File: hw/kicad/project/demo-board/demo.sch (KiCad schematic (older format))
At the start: 2 parts

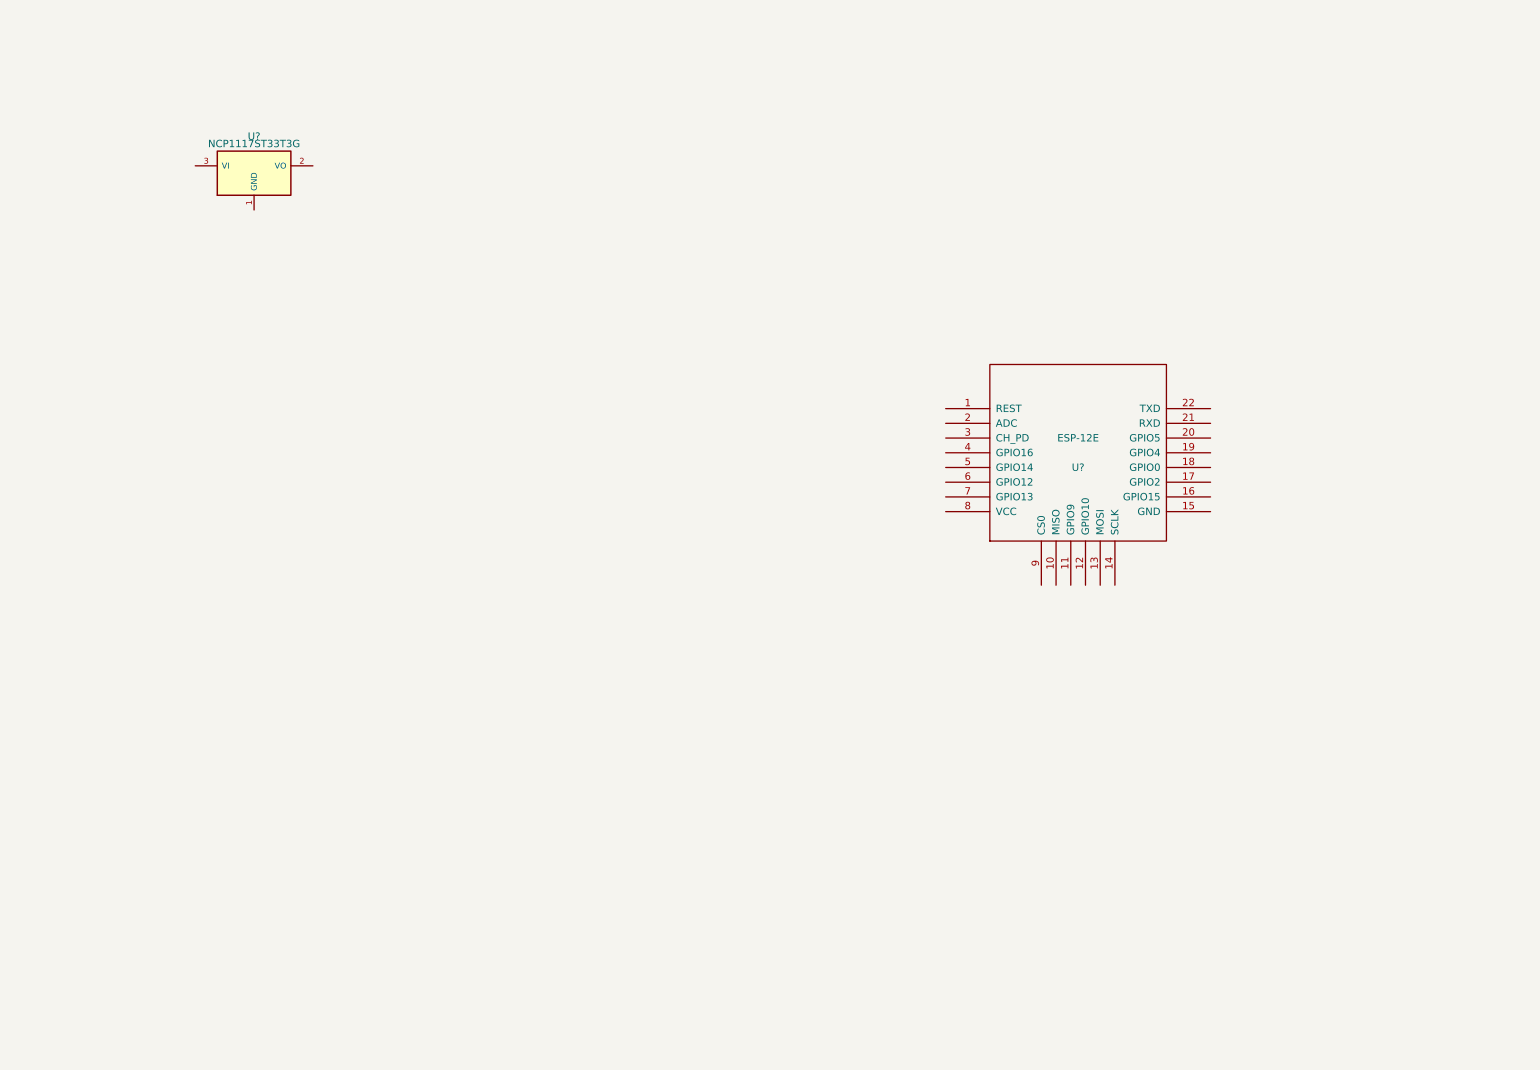
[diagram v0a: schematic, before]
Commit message: Demo schema for ESP connections
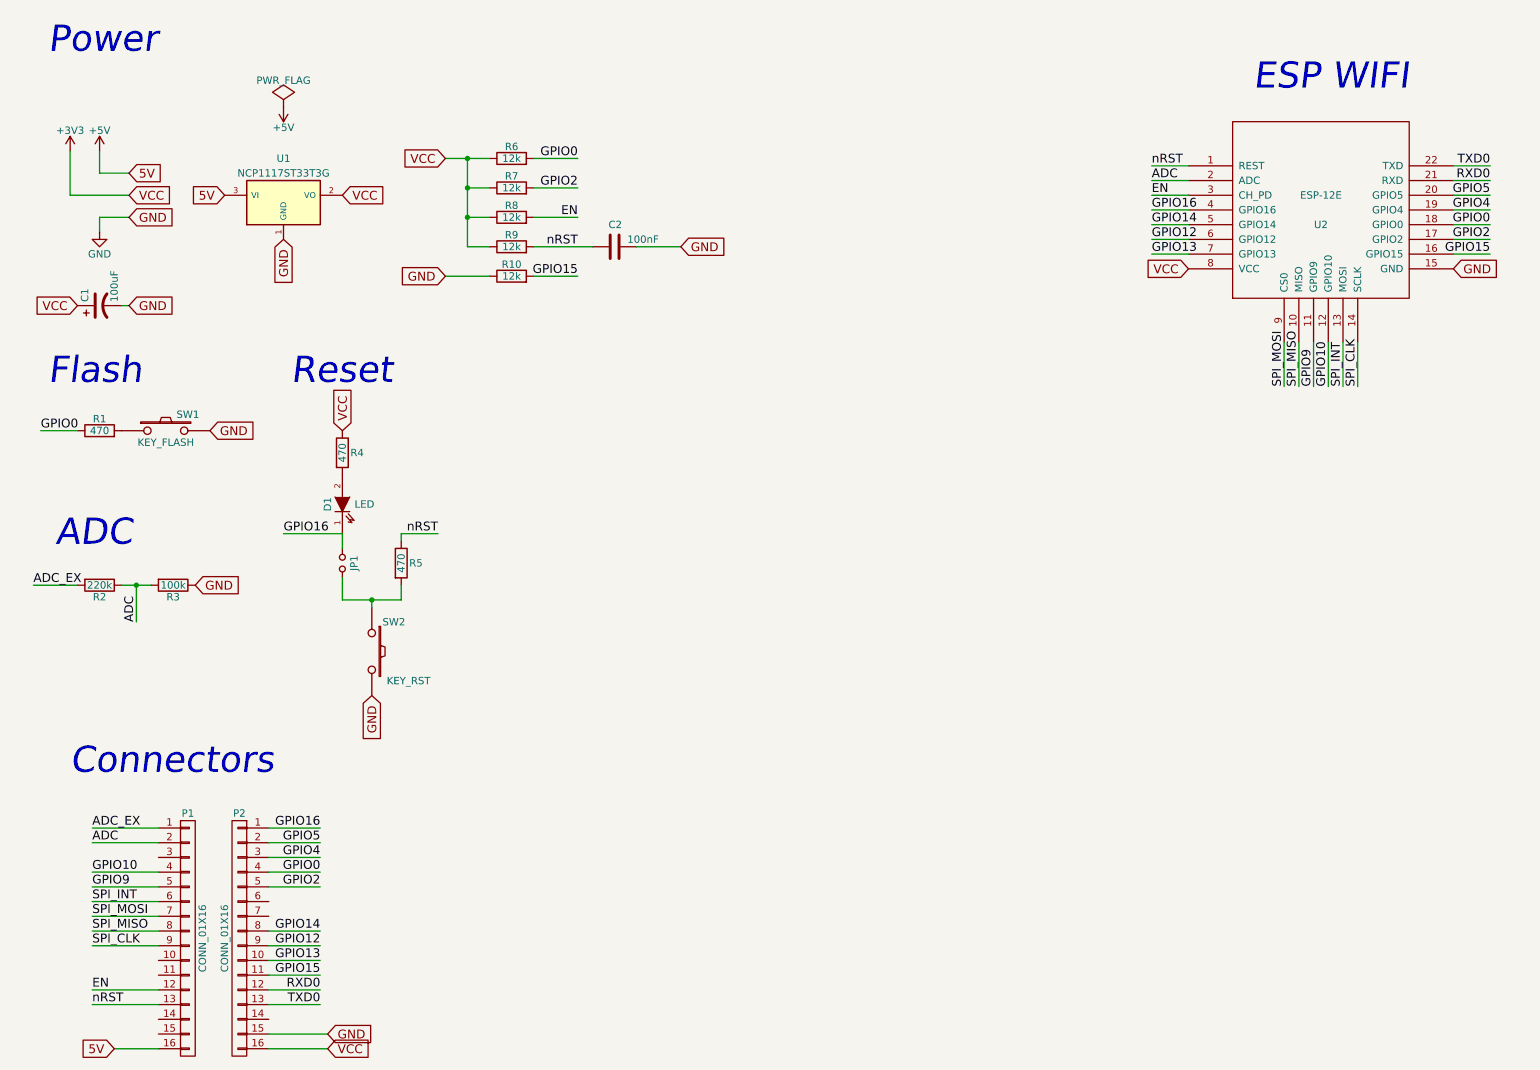
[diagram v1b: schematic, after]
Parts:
- added C1: 100uF, symbol CP1
- added C2: 100nF, symbol C
- added D1: LED, symbol LED
- added JP1: Jumper_NO_Small, symbol Jumper_NO_Small
- added P1, P2: CONN_01X16, symbol CONN_01X16
- added R1, R4, R5: 470, symbol R
- added R10, R6, R7, R8, R9: 12k, symbol R
- added R2: 220k, symbol R
- added R3: 100k, symbol R
- added SW1: KEY_FLASH, symbol SW_PUSH
- added SW2: KEY_RST, symbol SW_PUSH
- gave numbers to parts that had none: 2
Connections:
- net nRST: now reaches U2.1 (REST)
- net nRST: now also C2.1, P1.13 (P13), R5.1, R9.2
- net SPI_MISO: now reaches U2.10 (MISO)
- net SPI_MISO: now also P1.8 (P8)
- net GPIO9: now reaches U2.11 (GPIO9)
- net GPIO9: now also P1.5 (P5)
- net GPIO10: now reaches U2.12 (GPIO10)
- net GPIO10: now also P1.4 (P4)
- net SPI_INT: now reaches U2.13 (MOSI)
- net SPI_INT: now also P1.6 (P6)
- net SPI_CLK: now reaches U2.14 (SCLK)
- net SPI_CLK: now also P1.9 (P9)
- net GND: now reaches U2.15 (GND)
- net GND: now also U1.1 (GND), C1.2, C2.2, P2.15 (P15), R10.1, R3.1, SW1.2, SW2.2
- net GPIO15: now reaches U2.16 (GPIO15)
- net GPIO15: now also P2.11 (P11), R10.2
- net GPIO2: now reaches U2.17 (GPIO2)
- net GPIO2: now also P2.5 (P5), R7.2
- net GPIO0: now reaches U2.18 (GPIO0)
- net GPIO0: now also P2.4 (P4), R1.1, R6.2
- net GPIO4: now reaches U2.19 (GPIO4)
- net GPIO4: now also P2.3 (P3)
- net ADC: now reaches U2.2 (ADC)
- net ADC: now also P1.2 (P2), R2.1, R3.2
- net GPIO5: now reaches U2.20 (GPIO5)
- net GPIO5: now also P2.2 (P2)
- net RXD0: now reaches U2.21 (RXD)
- net RXD0: now also P2.12 (P12)
- net TXD0: now reaches U2.22 (TXD)
- net TXD0: now also P2.13 (P13)
- net EN: now reaches U2.3 (CH_PD)
- net EN: now also P1.12 (P12), R8.2
- net GPIO16: now reaches U2.4 (GPIO16)
- net GPIO16: now also D1.1 (K), JP1.1, P2.1 (P1)
- net GPIO14: now reaches U2.5 (GPIO14)
- net GPIO14: now also P2.8 (P8)
- net GPIO12: now reaches U2.6 (GPIO12)
- net GPIO12: now also P2.9 (P9)
- net GPIO13: now reaches U2.7 (GPIO13)
- net GPIO13: now also P2.10 (P10)
- net +3V3: now reaches U2.8 (VCC)
- net +3V3: now also U1.2 (VO), C1.1, P2.16 (P16), R4.1, R6.1, R7.1, R8.1, R9.1
- net SPI_MOSI: now reaches U2.9 (CS0)
- net SPI_MOSI: now also P1.7 (P7)
- net +5V: now reaches U1.3 (VI)
- net +5V: now also P1.16 (P16)
- new net: R1.2, SW1.1
- new net: D1.2 (A), R4.2
- new net: JP1.2, R5.2, SW2.1
- new net ADC_EX: P1.1 (P1), R2.2
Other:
- note added: "ADC\n"
- note added: "Connectors"
- note added: "ESP WIFI"
- note added: "Flash"
- note added: "Power"
- note added: "Reset"
- moved on the sheet: U1, U2

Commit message: Parts associated
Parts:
- C1: footprint (none) -> Capacitors_Tantalum_SMD:TantalC_SizeB_EIA-3528_Reflow
- C2: footprint (none) -> Capacitors_SMD:C_0402
- D1: footprint (none) -> LEDs:LED-1206
- JP1: footprint (none) -> Pin_Headers:Pin_Header_Straight_1x02
- P1, P2: footprint (none) -> Pin_Headers:Pin_Header_Straight_1x16
- R1, R10, R2, R3, R4, R5, R6, R7, R8, R9: footprint (none) -> Resistors_SMD:R_1206
- SW1, SW2: footprint (none) -> Buttons_Switches_ThroughHole:SW_PUSH-12mm
- U1: footprint (none) -> TO_SOT_Packages_SMD:SOT-223
- U2: footprint (none) -> ESP8266:ESP-12E
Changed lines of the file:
@@
 F 0 "U2" H 9450 1850 50  0000 C CNN
 F 1 "ESP-12E" H 9450 2050 50  0000 C CNN
-F 2 "" H 9450 1950 50  0001 C CNN
+F 2 "ESP8266:ESP-12E" H 9450 1950 50  0001 C CNN
 F 3 "" H 9450 1950 50  0001 C CNN
 	1    9450 1950
@@
 F 0 "U1" H 2400 2200 50  0000 C CNN
 F 1 "NCP1117ST33T3G" H 2400 2100 50  0000 C CNN
-F 2 "" H 2400 1900 50  0000 C CNN
+F 2 "TO_SOT_Packages_SMD:SOT-223" H 2400 1900 50  0001 C CNN
 F 3 "" H 2400 1900 50  0000 C CNN
 	1    2400 1900
@@
 F 0 "R6" V 4030 1600 50  0000 C CNN
 F 1 "12k" V 3950 1600 50  0000 C CNN
-F 2 "" V 3880 1600 50  0000 C CNN
+F 2 "Resistors_SMD:R_1206" V 3880 1600 50  0001 C CNN
 F 3 "" H 3950 1600 50  0000 C CNN
 	1    3950 1600
@@
 F 0 "R7" V 4030 1800 50  0000 C CNN
 F 1 "12k" V 3950 1800 50  0000 C CNN
-F 2 "" V 3880 1800 50  0000 C CNN
+F 2 "Resistors_SMD:R_1206" V 3880 1800 50  0001 C CNN
 F 3 "" H 3950 1800 50  0000 C CNN
 	1    3950 1800
@@
 F 0 "R8" V 4030 2000 50  0000 C CNN
 F 1 "12k" V 3950 2000 50  0000 C CNN
-F 2 "" V 3880 2000 50  0000 C CNN
+F 2 "Resistors_SMD:R_1206" V 3880 2000 50  0001 C CNN
 F 3 "" H 3950 2000 50  0000 C CNN
 	1    3950 2000
@@
 F 0 "R9" V 4030 2200 50  0000 C CNN
 F 1 "12k" V 3950 2200 50  0000 C CNN
-F 2 "" V 3880 2200 50  0000 C CNN
+F 2 "Resistors_SMD:R_1206" V 3880 2200 50  0001 C CNN
 F 3 "" H 3950 2200 50  0000 C CNN
 	1    3950 2200
@@
 F 0 "R10" V 4030 2400 50  0000 C CNN
 F 1 "12k" V 3950 2400 50  0000 C CNN
-F 2 "" V 3880 2400 50  0000 C CNN
+F 2 "Resistors_SMD:R_1206" V 3880 2400 50  0001 C CNN
 F 3 "" H 3950 2400 50  0000 C CNN
 	1    3950 2400
@@
 F 0 "C1" H 1175 2700 50  0000 L CNN
 F 1 "100uF" H 1175 2500 50  0000 L CNN
-F 2 "" H 1150 2600 50  0000 C CNN
+F 2 "Capacitors_Tantalum_SMD:TantalC_SizeB_EIA-3528_Reflow" H 1150 2600 50  0001 C CNN
 F 3 "" H 1150 2600 50  0000 C CNN
 	1    1150 2600
@@
 F 0 "R1" V 1230 3450 50  0000 C CNN
 F 1 "470" V 1150 3450 50  0000 C CNN
-F 2 "" V 1080 3450 50  0000 C CNN
+F 2 "Resistors_SMD:R_1206" V 1080 3450 50  0001 C CNN
 F 3 "" H 1150 3450 50  0000 C CNN
 	1    1150 3450
@@
 F 0 "SW1" H 1750 3560 50  0000 C CNN
 F 1 "KEY_FLASH" H 1600 3370 50  0000 C CNN
-F 2 "" H 1600 3450 50  0000 C CNN
+F 2 "Buttons_Switches_ThroughHole:SW_PUSH-12mm" H 1600 3450 50  0001 C CNN
 F 3 "" H 1600 3450 50  0000 C CNN
 	1    1600 3450
@@
 F 0 "R4" H 2900 3600 50  0000 C CNN
 F 1 "470" V 2800 3600 50  0000 C CNN
-F 2 "" V 2730 3600 50  0000 C CNN
+F 2 "Resistors_SMD:R_1206" V 2730 3600 50  0001 C CNN
 F 3 "" H 2800 3600 50  0000 C CNN
 	1    2800 3600
@@
 F 0 "D1" H 2800 4050 50  0000 C CNN
 F 1 "LED" V 2800 3800 50  0000 C CNN
-F 2 "" H 2800 3950 50  0000 C CNN
+F 2 "LEDs:LED-1206" H 2800 3950 50  0001 C CNN
 F 3 "" H 2800 3950 50  0000 C CNN
 	1    2800 3950
@@
 F 0 "JP1" H 2800 4430 50  0000 C CNN
 F 1 "Jumper_NO_Small" H 2810 4290 50  0001 C CNN
-F 2 "" H 2800 4350 50  0000 C CNN
+F 2 "Pin_Headers:Pin_Header_Straight_1x02" H 2800 4350 50  0001 C CNN
 F 3 "" H 2800 4350 50  0000 C CNN
 	1    2800 4350
@@
 F 0 "R5" H 3300 4350 50  0000 C CNN
 F 1 "470" V 3200 4350 50  0000 C CNN
-F 2 "" V 3130 4350 50  0000 C CNN
+F 2 "Resistors_SMD:R_1206" V 3130 4350 50  0001 C CNN
 F 3 "" H 3200 4350 50  0000 C CNN
 	1    3200 4350
@@
 F 0 "SW2" V 2800 5100 50  0000 C CNN
 F 1 "KEY_RST" V 3200 5200 50  0000 C CNN
-F 2 "" H 3000 4950 50  0000 C CNN
+F 2 "Buttons_Switches_ThroughHole:SW_PUSH-12mm" H 3000 4950 50  0001 C CNN
 F 3 "" H 3000 4950 50  0000 C CNN
 	1    3000 4950
@@
 F 0 "R2" V 1230 4500 50  0000 C CNN
 F 1 "220k" V 1150 4500 50  0000 C CNN
-F 2 "" V 1080 4500 50  0000 C CNN
+F 2 "Resistors_SMD:R_1206" V 1080 4500 50  0001 C CNN
 F 3 "" H 1150 4500 50  0000 C CNN
 	1    1150 4500
@@
 F 0 "R3" V 1730 4500 50  0000 C CNN
 F 1 "100k" V 1650 4500 50  0000 C CNN
-F 2 "" V 1580 4500 50  0000 C CNN
+F 2 "Resistors_SMD:R_1206" V 1580 4500 50  0001 C CNN
 F 3 "" H 1650 4500 50  0000 C CNN
 	1    1650 4500
@@
 F 0 "P1" H 1750 7750 50  0000 C CNN
 F 1 "CONN_01X16" V 1850 6900 50  0000 C CNN
-F 2 "" H 1750 6900 50  0000 C CNN
+F 2 "Pin_Headers:Pin_Header_Straight_1x16" H 1750 6900 50  0001 C CNN
 F 3 "" H 1750 6900 50  0000 C CNN
 	1    1750 6900
@@
 F 0 "P2" H 2100 7750 50  0000 C CNN
 F 1 "CONN_01X16" V 2200 6900 50  0000 C CNN
-F 2 "" H 2100 6900 50  0000 C CNN
+F 2 "Pin_Headers:Pin_Header_Straight_1x16" H 2100 6900 50  0001 C CNN
 F 3 "" H 2100 6900 50  0000 C CNN
 	1    2100 6900
@@
 F 0 "C2" V 4800 2150 50  0000 L CNN
 F 1 "100nF" V 4700 1900 50  0000 L CNN
-F 2 "" H 4688 2050 50  0000 C CNN
+F 2 "Capacitors_SMD:C_0402" H 4688 2050 50  0001 C CNN
 F 3 "" H 4650 2200 50  0000 C CNN
 	1    4650 2200

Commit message: Draft PCB added
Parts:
- SW1, SW2: footprint Buttons_Switches_ThroughHole:SW_PUSH-12mm -> Buttons_Switches_ThroughHole:SW_PUSH_SMALL
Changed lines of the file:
@@
 LIBS:contrib
 LIBS:valves
+LIBS:demo-cache
 EELAYER 25 0
 EELAYER END
@@
 F 0 "SW1" H 1750 3560 50  0000 C CNN
 F 1 "KEY_FLASH" H 1600 3370 50  0000 C CNN
-F 2 "Buttons_Switches_ThroughHole:SW_PUSH-12mm" H 1600 3450 50  0001 C CNN
+F 2 "Buttons_Switches_ThroughHole:SW_PUSH_SMALL" H 1600 3450 50  0001 C CNN
 F 3 "" H 1600 3450 50  0000 C CNN
 	1    1600 3450
@@
 F 0 "SW2" V 2800 5100 50  0000 C CNN
 F 1 "KEY_RST" V 3200 5200 50  0000 C CNN
-F 2 "Buttons_Switches_ThroughHole:SW_PUSH-12mm" H 3000 4950 50  0001 C CNN
+F 2 "Buttons_Switches_ThroughHole:SW_PUSH_SMALL" H 3000 4950 50  0001 C CNN
 F 3 "" H 3000 4950 50  0000 C CNN
 	1    3000 4950

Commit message: Added SD card and 3d shapes
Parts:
- added J1: MicroSD, armory:MICRO_SD_HINGE_AMP, symbol MicroSD
- U2: footprint ESP8266:ESP-12E -> armory_new:ESP-12E_with_3d
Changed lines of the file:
@@
 EESchema Schematic File Version 2
+LIBS:DataStorage
 LIBS:ESP8266
 LIBS:power
@@
 F 0 "U2" H 9450 1850 50  0000 C CNN
 F 1 "ESP-12E" H 9450 2050 50  0000 C CNN
-F 2 "ESP8266:ESP-12E" H 9450 1950 50  0001 C CNN
+F 2 "armory_new:ESP-12E_with_3d" H 9450 1950 50  0001 C CNN
 F 3 "" H 9450 1950 50  0001 C CNN
 	1    9450 1950
@@
 Wire Wire Line
 	2300 7250 2650 7250
+$Comp
+L MicroSD J1
+U 1 1 5676DE33
+P 4800 6200
+F 0 "J1" H 4600 6900 60  0000 C CNN
+F 1 "MicroSD" H 4600 5500 60  0000 C CNN
+F 2 "armory:MICRO_SD_HINGE_AMP" H 4900 6350 60  0001 C CNN
+F 3 "" H 4900 6350 60  0000 C CNN
+	1    4800 6200
+	1    0    0    -1
+$EndComp
 $EndSCHEMATC

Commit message: Improve library management
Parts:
- removed J1: MicroSD, armory:MICRO_SD_HINGE_AMP, symbol MicroSD
- added J2: MICRO_SD_HINGE, armory_local:MICRO_SD_HINGE_AMP, symbol MICRO_SD_HINGE
- U2: footprint armory_new:ESP-12E_with_3d -> ESP8266_local:ESP-12E_with_3d
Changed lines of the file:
@@
 EESchema Schematic File Version 2
-LIBS:DataStorage
-LIBS:ESP8266
 LIBS:power
 LIBS:device
@@
 LIBS:contrib
 LIBS:valves
+LIBS:ESP8266
+LIBS:DataStorage
+LIBS:armory
 LIBS:demo-cache
 EELAYER 25 0
@@
 F 0 "U2" H 9450 1850 50  0000 C CNN
 F 1 "ESP-12E" H 9450 2050 50  0000 C CNN
-F 2 "armory_new:ESP-12E_with_3d" H 9450 1950 50  0001 C CNN
+F 2 "ESP8266_local:ESP-12E_with_3d" H 9450 1950 50  0001 C CNN
 F 3 "" H 9450 1950 50  0001 C CNN
 	1    9450 1950
@@
 	2300 7250 2650 7250
 $Comp
-L MicroSD J1
-U 1 1 5676DE33
-P 4800 6200
-F 0 "J1" H 4600 6900 60  0000 C CNN
-F 1 "MicroSD" H 4600 5500 60  0000 C CNN
-F 2 "armory:MICRO_SD_HINGE_AMP" H 4900 6350 60  0001 C CNN
-F 3 "" H 4900 6350 60  0000 C CNN
-	1    4800 6200
-	1    0    0    -1
-$EndComp
+L MICRO_SD_HINGE J2
+U 1 1 56772422
+P 6100 6150
+F 0 "J2" H 6150 6200 60  0000 C CNN
+F 1 "MICRO_SD_HINGE" H 6100 6700 60  0000 C CNN
+F 2 "armory_local:MICRO_SD_HINGE_AMP" V 6210 5650 60  0001 C CNN
+F 3 "" V 6210 5650 60  0000 C CNN
+	1    6100 6150
+	1    0    0    -1
+$EndComp

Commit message: Intermediate commit
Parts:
- removed P1, P2: CONN_01X16, Pin_Headers:Pin_Header_Straight_1x16, symbol CONN_01X16
- added P?: CONN_01X03, symbol CONN_01X03
- added P? (x2): CONN_01X08, symbol CONN_01X07
- added P?: CONN_01X06, symbol CONN_01X06
- added P? (x2): CONN_01X08, symbol CONN_01X08
- added R? (x5): 50k, Resistors_SMD:R_1206, symbol R
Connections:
- net +3V3: now also J2.4 (VDD), P?.3 (P3), P?.6 (P6), R?.1, R?.1, R?.1, R?.1, R?.1
- net +5V: now also P?.2 (P2)
- net ADC: now also P?.2 (P2)
- net EN: now also P?.3 (P3)
- net GND: now also J2.10 (GND2), J2.11 (GND3), J2.12 (GND4), J2.6 (VSS), J2.9 (GND1), P?.1 (P1), P?.8 (P8)
- net GPIO0: now also P?.3 (P3)
- net GPIO10: now also P?.4 (P4)
- net GPIO12: now also P?.6 (P6)
- net GPIO13: now also P?.7 (P7)
- net GPIO14: now also P?.5 (P5)
- net GPIO15: now also P?.1 (P1)
- net GPIO16: now also P?.4 (P4)
- net GPIO2: now also P?.2 (P2)
- net GPIO4: now also P?.4 (P4)
- net GPIO5: now also P?.5 (P5)
- net GPIO9: now also P?.3 (P3)
- net RXD0: now also P?.6 (P6)
- net SPI_CLK: now also P?.6 (P6)
- net SPI_INT: now also P?.5 (P5)
- net SPI_MISO: now also P?.2 (P2)
- net SPI_MOSI: now also P?.1 (P1)
- net TXD0: now also P?.7 (P7)
- net nRST: now also P?.1 (P1)
- net at J2.1 (DAT2): now also R?.2
- net SD_CS: now reaches J2.2 (CD/DAT3)
- net SD_CS: now also R?.2
- net SD_LCD_MOSI: now reaches J2.3 (CMD)
- net SD_LCD_MOSI: now also P?.4 (P4), R?.2
- net SD_LCD_CLK: now reaches J2.5 (CLK)
- net SD_LCD_CLK: now also P?.5 (P5)
- net SD_LCD_MISO: now reaches J2.7 (DAT0)
- net SD_LCD_MISO: now also R?.2
- net at J2.8 (DAT1): now also R?.2
- new net LCD_CS: P?.2 (P2)
- new net LCD_LED: P?.7 (P7)
- new net LCD_RST: P?.1 (P1)
- new net SD_LCD_DATA_CMD: P?.3 (P3)
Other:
- note added: "LCD"
- note added: "SD card"
- moved on the sheet: U2

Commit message: Schematic clarified
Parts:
- removed D1: LED, LEDs:LED-1206, symbol LED
- removed R4, R5: 470, Resistors_SMD:R_1206, symbol R
- added C?: 1nF, Capacitors_SMD:C_0402, symbol C
- gave numbers to parts that had none: 11
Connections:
- net +3V3: now also C?.1
- net GND: now also C?.2
- net GPIO16: no longer JP1.1
- net nRST: now also JP1.1
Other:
- moved on the sheet: JP1, R1, R2, R3, SW1, SW2

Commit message: Board routes part 1
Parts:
- removed P6: CONN_01X08, symbol CONN_01X08
- added P6: SD_LCD_CONN, Pin_Headers:Pin_Header_Straight_1x07, symbol CONN_01X07
- P1, P3: value CONN_01X08 -> ESP_CONN; footprint (none) -> Pin_Headers:Pin_Header_Straight_1x07
- P2: value CONN_01X06 -> ESP_CONN; footprint (none) -> Pin_Headers:Pin_Header_Straight_1x07; symbol CONN_01X06 -> CONN_01X07
- P4: value CONN_01X03 -> PWR_CONN; footprint (none) -> Pin_Headers:Pin_Header_Straight_1x03
- P5: value CONN_01X08 -> CONN_DISPLAY; footprint (none) -> display_local:Nokia_5110_LCD; symbol CONN_01X08 -> CONN_DISPLAY
- gave numbers to parts that had none: 1
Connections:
- net ADC_EX: now also P2.1 (P1)
- net GPIO10: now also P2.5 (P5); no longer P2.4 (P4)
- net GPIO9: now also P2.4 (P4); no longer P2.3 (P3)
- net LCD_CS: now also P6.2 (P2)
- net LCD_LED: now also P6.6 (P6)
- net LCD_RST: now also P6.1 (P1)
- net SD_CS: now also P6.7 (P7)
- net SD_LCD_CLK: now also P6.5 (P5)
- net SD_LCD_DATA_CMD: now also P6.3 (P3)
- net SD_LCD_MOSI: now also P6.4 (P4)
- net SPI_CLK: now also P2.7 (P7); no longer P2.6 (P6)
- net SPI_INT: now also P2.6 (P6); no longer P2.5 (P5)
- net SPI_MISO: now also P2.3 (P3); no longer P2.2 (P2)
- net SPI_MOSI: now also P2.2 (P2); no longer P2.1 (P1)
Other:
- moved on the sheet: P5, U2
